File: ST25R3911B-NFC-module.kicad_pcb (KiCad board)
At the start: 2 copper layers, 81.2 x 36.8 mm, 52 parts, among them J1 USB_C_Receptacle_USB2.0_16P, SW1 B3U1000P, SW2 SW_Push, SW3 SW_Push, U1 ST25R3911B-AQF, U2 AP1117-33, U3 W25Q128JVS, U4 RP2040, U5 nRF24L01P, Y1 Crystal_GND24

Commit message: схему вроде сделал, надо только понять как вообще адекватно, а главное симметрично мне провести к антенне всё что надобно
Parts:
- removed D1, D2, D3, D4: LED, LED_SMD:LED_0402_1005Metric
- removed DD1: IP5306, Package_SO:HSOP-8-1EP_3.9x4.9mm_P1.27mm_EP2.3x2.3mm
- removed REF**: COIL_GENERATOR, COIL_GENERATOR
- removed SW3: SW_Push, Button_Switch_SMD:SW_SPST_B3U-1000P
- added ANT1: ~, NFC_ant:Без имени, F.Cu at (86.8, 100.2)
- added C23: 12pF, Capacitor_SMD:C_0402_1005Metric, F.Cu at (80.8, 83.0)
- added C24: 27pF, Capacitor_SMD:C_0402_1005Metric, F.Cu at (79.0, 86.2)
- added C25: 56pF, Capacitor_SMD:C_0402_1005Metric, F.Cu at (77.2, 86.2)
- added C26: 100nF, Capacitor_SMD:C_0402_1005Metric, F.Cu at (70.8, 77.1)
- added C27: 100nF, Capacitor_SMD:C_0402_1005Metric, F.Cu at (71.8, 85.7)
- added C28: 10uF, Capacitor_SMD:C_0402_1005Metric, F.Cu at (72.7, 85.7)
- added C29: 680pF, Capacitor_SMD:C_0402_1005Metric, F.Cu at (74.0, 91.7)
- added C30: 680pF, Capacitor_SMD:C_0402_1005Metric, F.Cu at (76.7, 89.0)
- added C31: 100nF, Capacitor_SMD:C_0402_1005Metric, F.Cu at (82.7, 76.4)
- added C32: 150pF, Capacitor_SMD:C_0402_1005Metric, F.Cu at (75.2, 94.3)
- added C33: 10pF, Capacitor_SMD:C_0402_1005Metric, F.Cu at (76.5, 93.7)
- added C34: 150pF, Capacitor_SMD:C_0402_1005Metric, F.Cu at (75.2, 93.0)
- added C35: 150pF, Capacitor_SMD:C_0402_1005Metric, F.Cu at (78.0, 90.2)
- added C36: 10pF, Capacitor_SMD:C_0402_1005Metric, F.Cu at (78.7, 91.5)
- added C37: 150pF, Capacitor_SMD:C_0402_1005Metric, F.Cu at (79.3, 90.2)
- added C38: 22uF, Capacitor_SMD:C_0402_1005Metric, F.Cu at (83.6, 76.4)
- added C39: 100nF, Capacitor_SMD:C_0402_1005Metric, F.Cu at (69.0, 87.7)
- added C40: 270pF, Capacitor_SMD:C_0402_1005Metric, F.Cu at (76.0, 92.3)
- added C41: 270pF, Capacitor_SMD:C_0402_1005Metric, F.Cu at (77.3, 91.0)
- added C42: 22uF, Capacitor_SMD:C_0402_1005Metric, F.Cu at (69.0, 88.7)
- added C43: 100nF, Capacitor_SMD:C_0402_1005Metric, F.Cu at (69.0, 83.9)
- added C44: 22uF, Capacitor_SMD:C_0402_1005Metric, F.Cu at (69.0, 84.8)
- added C45: 100nF, Capacitor_SMD:C_0402_1005Metric, F.Cu at (70.9, 79.5)
- added C46: 22uF, Capacitor_SMD:C_0402_1005Metric, F.Cu at (70.9, 78.5)
- added L2: LQW18ANR27G00D, Inductor_SMD:L_0603_1608Metric, F.Cu at (74.4, 90.5)
- added L3: LQW18ANR27G00D, Inductor_SMD:L_0603_1608Metric, F.Cu at (75.5, 89.4)
- added R10: 10K, PCM_Resistor_SMD_AKL:R_0402_1005Metric, F.Cu at (39.8, 90.9)
- added R11: CRF0805-FZ-R010ELF, PCM_Resistor_SMD_AKL:R_0805_2012Metric, F.Cu at (67.0, 83.6)
- added R12: 1K, PCM_Resistor_SMD_AKL:R_0402_1005Metric, F.Cu at (39.8, 93.0)
- added R13: 100K, PCM_Resistor_SMD_AKL:R_0402_1005Metric, F.Cu at (39.8, 95.1)
- added R14: 0R, PCM_Resistor_SMD_AKL:R_0402_1005Metric, F.Cu at (74.8, 75.4)
- added R15: 0R, PCM_Resistor_SMD_AKL:R_0402_1005Metric, F.Cu at (73.6, 75.4)
- added R16: 0R, PCM_Resistor_SMD_AKL:R_0402_1005Metric, F.Cu at (72.5, 75.4)
- added R17: 0R, PCM_Resistor_SMD_AKL:R_0402_1005Metric, F.Cu at (71.3, 75.4)
- added R18: 0R, PCM_Resistor_SMD_AKL:R_0402_1005Metric, F.Cu at (77.0, 75.4)
- added R19: 0R, PCM_Resistor_SMD_AKL:R_0402_1005Metric, F.Cu at (75.8, 75.4)
- added R20: 1R3, PCM_Resistor_SMD_AKL:R_0402_1005Metric, F.Cu at (78.1, 94.3)
- added R21: 1R3, PCM_Resistor_SMD_AKL:R_0402_1005Metric, F.Cu at (79.3, 93.0)
- added TP5: CSI, TestPoint:TestPoint_Pad_D1.0mm, F.Cu at (84.2, 74.2)
- added TP6: CSO, TestPoint:TestPoint_Pad_D1.0mm, F.Cu at (68.8, 77.8)
- added Y2: WTL2M85589FO, Crystal:Crystal_SMD_2520-4Pin_2.5x2.0mm, F.Cu at (69.8, 81.5)
- C1, C3, C7: value 22uF -> 100nF
- C10: value 100nF -> 22uF
- C15: value 15pF -> 22uF
- C16: value 15pF -> 8pF
- C17: value 22uF -> 8pF
- C18, C22: value 22uF -> 5.6pF
- C19: value 22uF -> 12pF
- C20: value 22uF -> 27pF
- C21: value 22uF -> 56pF
- C5: value 10uF -> 15pF
- C6: value 100nF -> 10uF
- C9: value 22uF -> 15pF
- L1: value LQH32CN1R0M33L -> LQG18HN2N7S00D; footprint Inductor_SMD:L_1210_3225Metric -> Inductor_SMD:L_0603_1608Metric
- R1: value 5.1K -> CRF0805-FZ-R010ELF; footprint PCM_Resistor_SMD_AKL:R_0402_1005Metric -> PCM_Resistor_SMD_AKL:R_0805_2012Metric_Pad1.15x1.40mm
- R2: value 5.1K -> 1K
- R3: value 10K -> 5.1K
- R4: value 0.5R -> 5.1K
- R7: value 27R -> 100K
- R9: value 10K -> 27R
- SW1: value B3U1000P -> SW_Push
- TP1: value BAT+ -> SWCLK; footprint TestPoint:TestPoint_Pad_D2.0mm -> TestPoint:TestPoint_Pad_D1.0mm
- TP2: value BAT- -> SWD; footprint TestPoint:TestPoint_Pad_D2.0mm -> TestPoint:TestPoint_Pad_D1.0mm
- TP3: value SWCLK -> ~; footprint TestPoint:TestPoint_Pad_D1.0mm -> TestPoint:TestPoint_Pad_1.5x1.5mm
- TP4: value SWD -> ~; footprint TestPoint:TestPoint_Pad_D1.0mm -> TestPoint:TestPoint_Pad_1.5x1.5mm
- U1: value ST25R3911B-AQF -> AP1117-33; footprint Package_DFN_QFN:QFN-32-1EP_5x5mm_P0.5mm_EP3.6x3.6mm_ThermalVias -> Package_TO_SOT_SMD:SOT-223-3_TabPin2
- U2: value AP1117-33 -> W25Q128JVS; footprint Package_TO_SOT_SMD:SOT-223-3_TabPin2 -> Package_SO:SOIC-8_5.3x5.3mm_P1.27mm
- U3: value W25Q128JVS -> LM358D; footprint Package_SO:SOIC-8_5.3x5.3mm_P1.27mm -> PCM_Package_SO_AKL:SO-8_3.9x4.9mm_P1.27mm
- U5: value nRF24L01P -> ST25R3911B-AQF; footprint Package_DFN_QFN:QFN-20-1EP_4x4mm_P0.5mm_EP2.5x2.5mm -> Package_DFN_QFN:QFN-32-1EP_5x5mm_P0.5mm_EP3.6x3.6mm_ThermalVias
- moved TP4 71.6 mm to (46.9, 64.5), turned to -90 degrees
- moved TP3 67.0 mm to (50.4, 64.5), turned to -90 degrees
- moved R9 65.9 mm to (39.8, 88.8)
- moved R7 64.8 mm to (36.8, 99.4)
- moved R8 64.8 mm to (36.8, 101.5)
- moved R4 63.2 mm to (36.8, 93.0)
- moved R5 63.2 mm to (36.8, 95.1)
- moved R6 63.2 mm to (36.8, 97.3)
- moved R3 62.3 mm to (36.8, 90.9)
- moved R2 62.3 mm to (36.8, 88.8)
- moved U1 61.6 mm to (54.5, 91.5), turned to 0 degrees
- moved TP2 59.7 mm to (45.8, 92.3)
- moved TP1 59.6 mm to (45.8, 89.2)
- moved J1 54.0 mm to (49.6, 57.5)
- moved U3 53.7 mm to (57.9, 69.8), turned to 90 degrees
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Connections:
- C1 pad 1: +5V -> +3.3V
- C10 pad 1: +3.3V -> Earth
- C10 pad 2: Earth -> Net-(U4-VREG_VOUT)
- C11 pad 1: Net-(DD1-BAT) -> Earth
- C11 pad 2: Earth -> Net-(U4-VREG_VOUT)
- C12 pad 1: Earth -> +3.3V
- C12 pad 2: +5V -> Earth
- C13 pad 1: Earth -> +3.3V
- C13 pad 2: +5V -> Earth
- C14 pad 1: Net-(C14-Pad1) -> +3.3V
- C15 pad 1: Net-(U4-XIN) -> +3.3V
- C16 pad 2: Net-(U4-XOUT) -> Net-(U5-XTO)
- C17 pad 1: Earth -> Net-(U5-XTI)
- C17 pad 2: Net-(U4-VREG_VOUT) -> Earth
- C18 pad 1: Earth -> TRIM1_0
- C18 pad 2: Net-(U4-VREG_VOUT) -> TRIM1
- C19 pad 1: +3.3V -> TRIM1_1
- C19 pad 2: Earth -> TRIM1
- C2 pad 1: +5V USB -> +5V DOMAIN
- C20 pad 1: +3.3V -> TRIM1_2
- C20 pad 2: Earth -> TRIM1
- C21 pad 1: +3.3V -> TRIM1_3
- C21 pad 2: Earth -> TRIM1
- C22 pad 1: +3.3V -> TRIM2_0
- C22 pad 2: Earth -> TRIM2
- C3 pad 1: +5V USB -> +3.3V
- C4 pad 1: +3.3V -> +3.3V_LDO
- C5 pad 1: +3.3V -> Net-(U4-XIN)
- C6 pad 1: +3.3V -> +3.3V_LDO
- C7 pad 1: +5V USB -> +3.3V_LDO
- C8 pad 1: Earth -> +5V USB
- C8 pad 2: +5V -> Earth
- C9 pad 2: +5V -> Net-(U4-XOUT)
- L1 pad 1: Net-(DD1-SW) -> +5V DOMAIN
- L1 pad 2: Net-(C14-Pad1) -> Net-(U5-VDD)
- R1 pad 1: Net-(J1-CC1) -> +5V USB
- R1 pad 2: Earth -> +5V DOMAIN
- R2 pad 1: Net-(J1-CC2) -> Net-(U3A--)
- R2 pad 2: Earth -> +5V DOMAIN
- R3 pad 1: Net-(DD1-KEY) -> Net-(J1-CC1)
- R3 pad 2: Net-(R3-Pad2) -> Earth
- R4 pad 1: Net-(DD1-BAT) -> Net-(J1-CC2)
- R4 pad 2: Net-(C14-Pad1) -> Earth
- R5 pad 1: Net-(U3-~{CS}) -> Net-(U2-~{CS})
- R6 pad 1: Net-(U3-~{CS}) -> Net-(U2-~{CS})
- R7 pad 1: Net-(U4-USB_DM) -> CURRENT_5V
- R7 pad 2: USB- -> Net-(U3A--)
- R8 pad 1: Net-(U4-USB_DP) -> Net-(U4-USB_DM)
- R8 pad 2: USB+ -> USB-
- R9 pad 1: Net-(U4-RUN) -> Net-(U4-USB_DP)
- R9 pad 2: +3.3V -> USB+
- SW1 pad 1: Net-(R3-Pad2) -> Earth
- SW1 pad 2: Earth -> Net-(R5-Pad2)
- SW2 pad 2: Net-(R5-Pad2) -> Net-(U4-RUN)
- TP1 pad 1: Net-(C14-Pad1) -> Net-(U4-SWCLK)
- TP2 pad 1: Earth -> Net-(U4-SWD)
- TP3 pad 1: Net-(U4-SWCLK) -> +5V USB
- TP4 pad 1: Net-(U4-SWD) -> Earth
- U1 pad 1: unconnected-(U1-VDD_IO-Pad1) -> Earth
- U1 pad 2: unconnected-(U1-CSO-Pad2) -> +3.3V_LDO
- U1 pad 3: unconnected-(U1-VSP_D-Pad3) -> +5V DOMAIN
- U2 pad 1: Earth -> Net-(U2-~{CS})
- U2 pad 2: +3.3V -> Net-(U2-DO/IO_{1})
- U2 pad 3: +5V -> Net-(U2-~{WP}/IO_{2})
- U3 pad 1: Net-(U3-~{CS}) -> CURRENT_5V
- U3 pad 2: Net-(U3-DO/IO_{1}) -> Net-(U3A--)
- U3 pad 3: Net-(U3-~{WP}/IO_{2}) -> +5V USB
- U3 pad 5: Net-(U3-DI/IO_{0}) -> +3.3V_LDO
- U3 pad 6: Net-(U3-CLK) -> Net-(U3B--)
- U3 pad 7: Net-(U3-~{HOLD}/~{RESET}/IO_{3}) -> CURRENT_3V3
- U4 pad 16: unconnected-(U4-GPIO13-Pad16) -> SCLK
- U4 pad 17: unconnected-(U4-GPIO14-Pad17) -> !SS
- U4 pad 18: unconnected-(U4-GPIO15-Pad18) -> MOSI
- U4 pad 27: unconnected-(U4-GPIO16-Pad27) -> MISO
- U4 pad 32: unconnected-(U4-GPIO21-Pad32) -> MCU_CLK
- U4 pad 34: unconnected-(U4-GPIO22-Pad34) -> IRQ
- U4 pad 51: Net-(U3-~{HOLD}/~{RESET}/IO_{3}) -> Net-(U2-~{HOLD}/~{RESET}/IO_{3})
- U4 pad 52: Net-(U3-CLK) -> Net-(U2-CLK)
- U4 pad 53: Net-(U3-DI/IO_{0}) -> Net-(U2-DI/IO_{0})
- U4 pad 54: Net-(U3-~{WP}/IO_{2}) -> Net-(U2-~{WP}/IO_{2})
- U4 pad 55: Net-(U3-DO/IO_{1}) -> Net-(U2-DO/IO_{1})
- U4 pad 56: Net-(U3-~{CS}) -> Net-(U2-~{CS})
- U5 pad 1: unconnected-(U5-CE-Pad1) -> +3.3V
- U5 pad 10: unconnected-(U5-XC1-Pad10) -> RFO1
- U5 pad 11: unconnected-(U5-VDD_PA-Pad11) -> RFO2
- U5 pad 12: unconnected-(U5-ANT1-Pad12) -> Earth
- U5 pad 13: unconnected-(U5-ANT2-Pad13) -> TRIM1_3
- U5 pad 14: unconnected-(U5-VSS-Pad14) -> TRIM2_3
- U5 pad 15: unconnected-(U5-VDD-Pad15) -> TRIM1_2
- U5 pad 16: unconnected-(U5-IREF-Pad16) -> TRIM2_2
- U5 pad 17: unconnected-(U5-VSS-Pad17) -> TRIM1_1
- U5 pad 18: unconnected-(U5-VDD-Pad18) -> TRIM2_1
- U5 pad 19: unconnected-(U5-DVDD-Pad19) -> TRIM1_0
- U5 pad 2: unconnected-(U5-CSN-Pad2) -> Net-(U5-CSO)
- U5 pad 20: unconnected-(U5-VSS-Pad20) -> TRIM2_0
- U5 pad 21: (no net) -> Earth
- U5 pad 3: unconnected-(U5-SCK-Pad3) -> Net-(U5-VSP_D)
- U5 pad 4: unconnected-(U5-MOSI-Pad4) -> Net-(U5-XTO)
- U5 pad 5: unconnected-(U5-MISO-Pad5) -> Net-(U5-XTI)
- U5 pad 6: unconnected-(U5-IRQ-Pad6) -> Earth
- U5 pad 7: unconnected-(U5-VDD-Pad7) -> Net-(U5-VSP_A)
- U5 pad 8: unconnected-(U5-VSS-Pad8) -> Net-(U5-VDD)
- U5 pad 9: unconnected-(U5-XC2-Pad9) -> Net-(U5-VSP_RF)
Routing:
- net Earth: track 0.00 -> 21.9 mm
- net TRIM1: track 0.00 -> 17.9 mm
- net TRIM2: track 0.00 -> 15.7 mm, vias 0 -> 4
- net Net-(U5-VSP_RF): track 0.00 -> 8.81 mm
- net Net-(U5-VDD): track 0.00 -> 8.04 mm
- net (no net): track 7.14 -> 0.00 mm, vias 1 -> 0
- net RFO1: track 0.00 -> 6.81 mm
- net Net-(U5-CSO): track 0.00 -> 6.68 mm
- net Net-(U5-VSP_A): track 0.00 -> 5.43 mm
- net Net-(U5-XTI): track 0.00 -> 5.35 mm
- net RFO2: track 0.00 -> 5.28 mm
- net RFI1: track 0.00 -> 5.24 mm
- net Net-(U5-/SS): track 0.00 -> 4.63 mm
- net Net-(U5-SCLK): track 0.00 -> 4.26 mm
- net Net-(U5-MOSI): track 0.00 -> 4.03 mm
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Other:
- board outline removed

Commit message: rev0 готова
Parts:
- added G***: LOGO, LOGO, F.Cu at (75.6, 109.8)
- added G***: LOGO, LOGO, B.Cu at (66.8, 70.8)
- added G***: LOGO, LOGO, B.Cu at (68.6, 86.7)
- added G***: LOGO, LOGO, B.Cu at (62.2, 111.6)
- added G***: LOGO, LOGO, B.Cu at (65.7, 53.1)
- added G***: LOGO, LOGO, B.Cu at (87.9, 54.0)
- added G***: LOGO, LOGO, B.Cu at (66.2, 119.1)
- added G***: LOGO, LOGO, B.Cu at (75.4, 108.0)
- added G***: LOGO, LOGO, B.Cu at (88.7, 111.2)
- added G***: LOGO, LOGO, B.Cu at (82.3, 86.8)
- added G***: LOGO, LOGO, B.Cu at (75.5, 83.2)
- added G***: LOGO, LOGO, B.Cu at (85.5, 119.0)
- added LED1: LED_0402, LED_SMD:LED_0402_1005Metric, F.Cu at (61.8, 50.4)
- added LED2: LED_0402, LED_SMD:LED_0402_1005Metric, F.Cu at (63.8, 50.4)
- added LED3: LED_0402, LED_SMD:LED_0402_1005Metric, F.Cu at (65.8, 50.4)
- added R22: 200R, PCM_Resistor_SMD_AKL:R_0402_1005Metric, F.Cu at (60.8, 50.5)
- added R23: 200R, PCM_Resistor_SMD_AKL:R_0402_1005Metric, F.Cu at (62.8, 50.5)
- added R24: 200R, PCM_Resistor_SMD_AKL:R_0402_1005Metric, F.Cu at (64.8, 50.5)
- added kibuzzard-680CEA90: G***, kibuzzard-680CEA90, B.Cu at (75.7, 59.6)
- added kibuzzard-680CEAEF: G***, kibuzzard-680CEAEF, B.Cu at (70.5, 65.2)
- moved R7 60.6 mm to (82.0, 59.0), turned to 90 degrees
- moved C7 60.1 mm to (90.0, 53.0), turned to 90 degrees
- moved C4 58.5 mm to (90.0, 50.8), turned to 90 degrees
- moved C6 58.3 mm to (90.0, 55.3), turned to -90 degrees
- moved R8 58.2 mm to (75.8, 58.3), turned to 90 degrees
- moved R13 56.4 mm to (83.0, 59.0), turned to 90 degrees
- moved R12 55.8 mm to (84.0, 59.0), turned to 90 degrees
- moved R2 53.3 mm to (81.0, 59.0), turned to 90 degrees
- moved R4 49.7 mm to (72.4, 58.3), turned to -90 degrees
- moved U1 49.1 mm to (84.9, 53.0)
- moved R3 49.1 mm to (73.5, 58.3), turned to -90 degrees
- moved C10 48.2 mm to (76.7, 59.8), turned to 180 degrees
- moved R6 47.1 mm to (59.4, 56.0), turned to -90 degrees
- moved R5 46.9 mm to (59.4, 54.1), turned to 90 degrees
- moved C2 46.9 mm to (81.5, 57.2)
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- renumbered TP3 to +5V, TP4 to GND, TP1 to SWCLK, TP2 to SWDT
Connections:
- U4 pad 12: unconnected-(U4-GPIO9-Pad12) -> Net-(U4-GPIO9)
- U4 pad 13: unconnected-(U4-GPIO10-Pad13) -> Net-(U4-GPIO10)
- U4 pad 14: unconnected-(U4-GPIO11-Pad14) -> Net-(U4-GPIO11)
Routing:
- net +3.3V: track 3.78 -> 140.3 mm, vias 0 -> 10
- net +5V DOMAIN: track 0.00 -> 43.3 mm, vias 0 -> 2
- net Net-(U4-RUN): track 0.00 -> 33.4 mm, vias 0 -> 2
- net Net-(U4-GPIO11): track 0.00 -> 31.2 mm
- net Earth: track 21.9 -> 51.7 mm, vias 0 -> 83
- net Net-(U4-GPIO10): track 0.00 -> 29.4 mm
- net Net-(U4-GPIO9): track 0.00 -> 29.1 mm
- net +5V USB: track 0.00 -> 29.0 mm
- net Net-(U2-~{CS}): track 0.00 -> 28.9 mm, vias 0 -> 2
- net +3.3V_LDO: track 0.00 -> 27.4 mm
- net Net-(U2-~{WP}/IO_{2}): track 0.00 -> 19.8 mm
- net Net-(U2-DO/IO_{1}): track 0.00 -> 16.7 mm
- net Net-(U4-VREG_VOUT): track 0.00 -> 15.1 mm, vias 0 -> 2
- net IRQ: track 0.00 -> 14.2 mm
- net RFI2: track 0.91 -> 15.1 mm, vias 0 -> 2
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- added copper zone on F.Cu, net +3.3V
- added copper zone on F.Cu, net +5V USB
- added copper zone on B.Cu, net Earth
- added copper zone on F.Cu, net Earth
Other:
- board outline added: 36 x 76 mm
- board text added: "SWCLK"
- board text added: "by @madjogger"

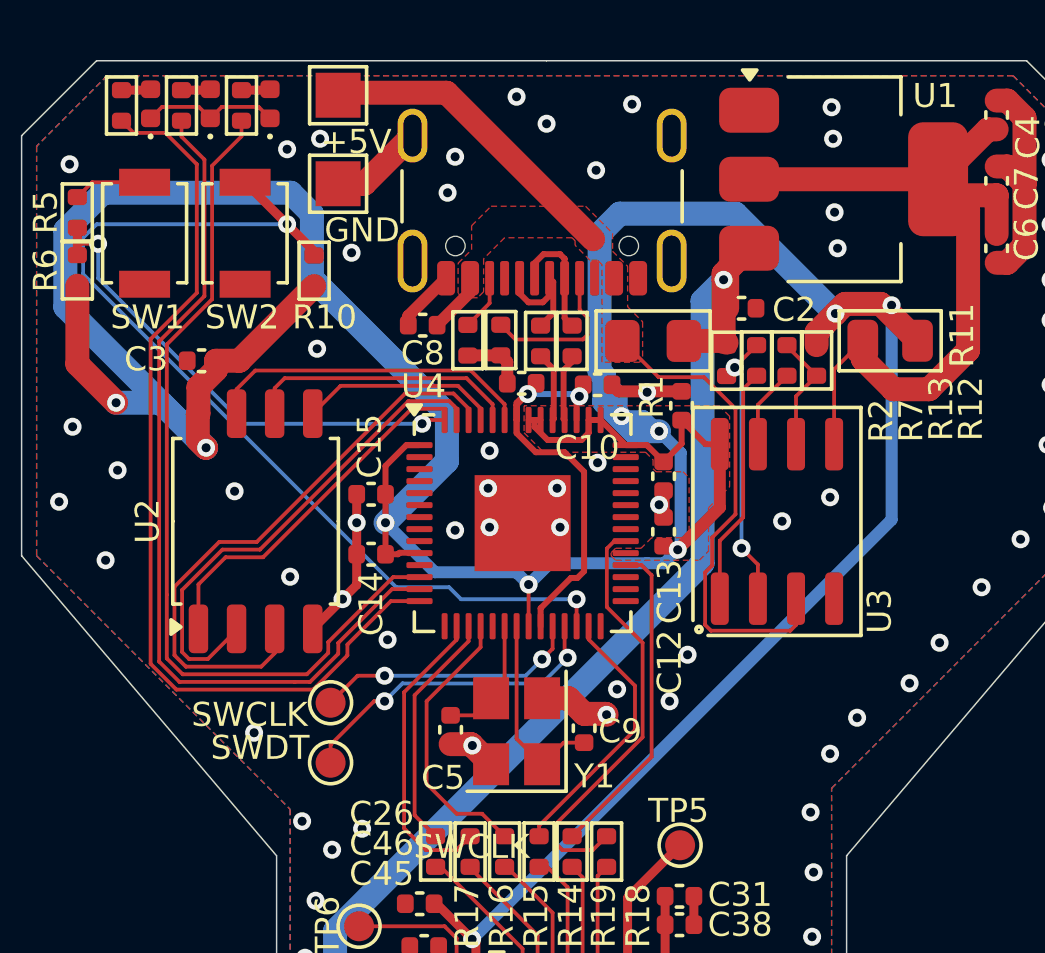
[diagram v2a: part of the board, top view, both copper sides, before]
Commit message: Довёл соединения для АЦП чтения потребления тока для доменов питания
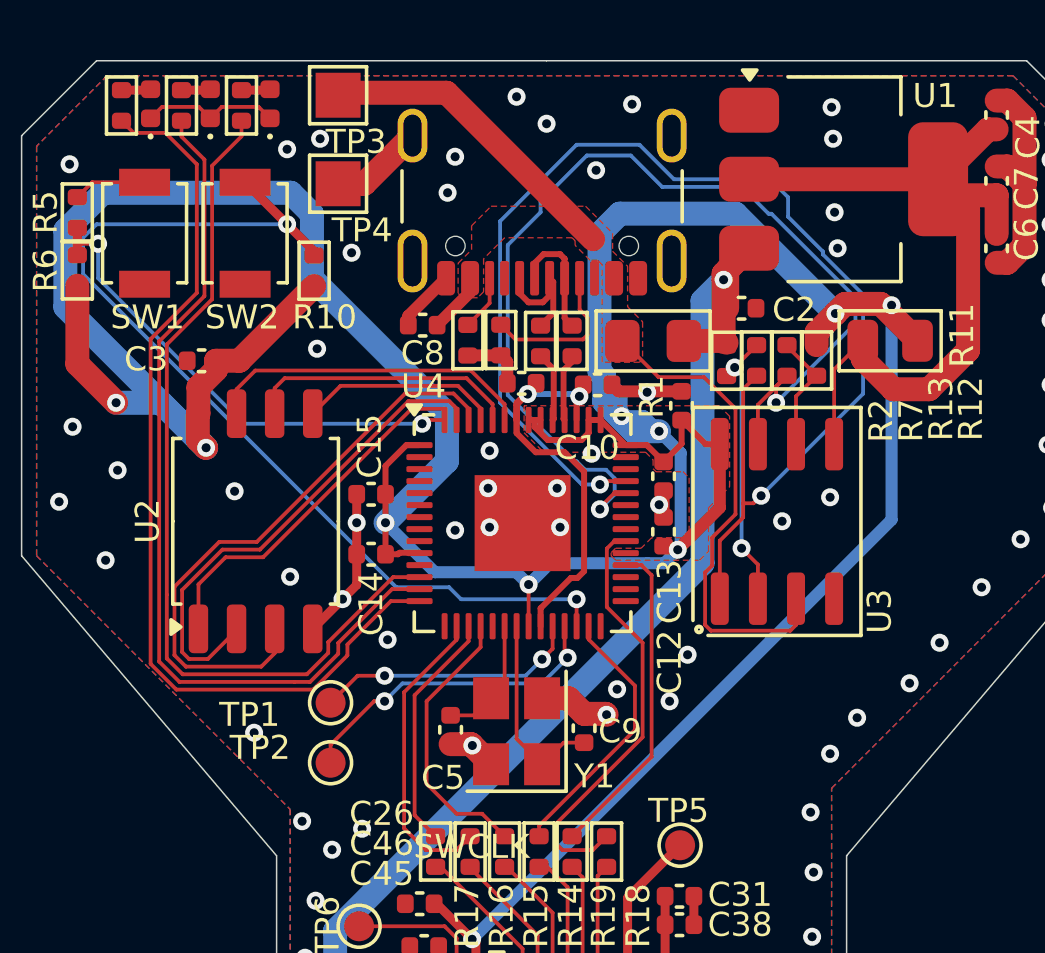
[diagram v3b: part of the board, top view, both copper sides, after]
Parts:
- renumbered SWCLK to TP1, SWDT to TP2, +5V to TP3, GND to TP4
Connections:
- U4 pad 38: unconnected-(U4-GPIO26_ADC0-Pad38) -> CURRENT_3V3
- U4 pad 39: unconnected-(U4-GPIO27_ADC1-Pad39) -> CURRENT_5V
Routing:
- net CURRENT_5V: track 7.94 -> 43.8 mm, vias 0 -> 2
- net CURRENT_3V3: track 2.68 -> 35.4 mm, vias 0 -> 2
